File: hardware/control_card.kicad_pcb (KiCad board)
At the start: 6 copper layers, 32.5 x 33.8 mm, 144 parts, among them J1 Power board, J2 JTAG, U1 A3CZ065BB18AE7S, U10 SN74LV4051APWR, U11 OPA365AIDBVR, U12 ADS7056IRUGR, U13 SN74LV4051APWR, U14 OPA365AIDBVR, U15 ADS7056IRUGR, U16 TLV75518PDBVR, U2 AP61302Z6-7, U3 AP61102Z6-7, U4 AP61102Z6-7, U5 TLV75512PDBVR, U6 TLV75533PDBVR, U7 MT25QU256ABA8E12-1SIT, U8 SN74AVC4T774RSVR, U9 W958D8NBYA5I, X1 100MHz

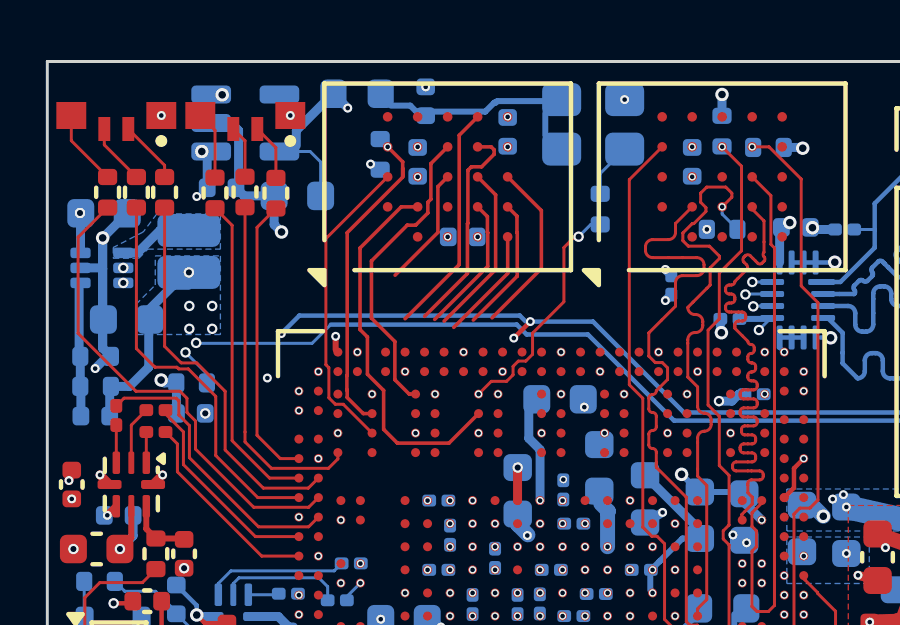
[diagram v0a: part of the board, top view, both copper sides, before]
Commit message: route hyperram to bank d for easier length matching
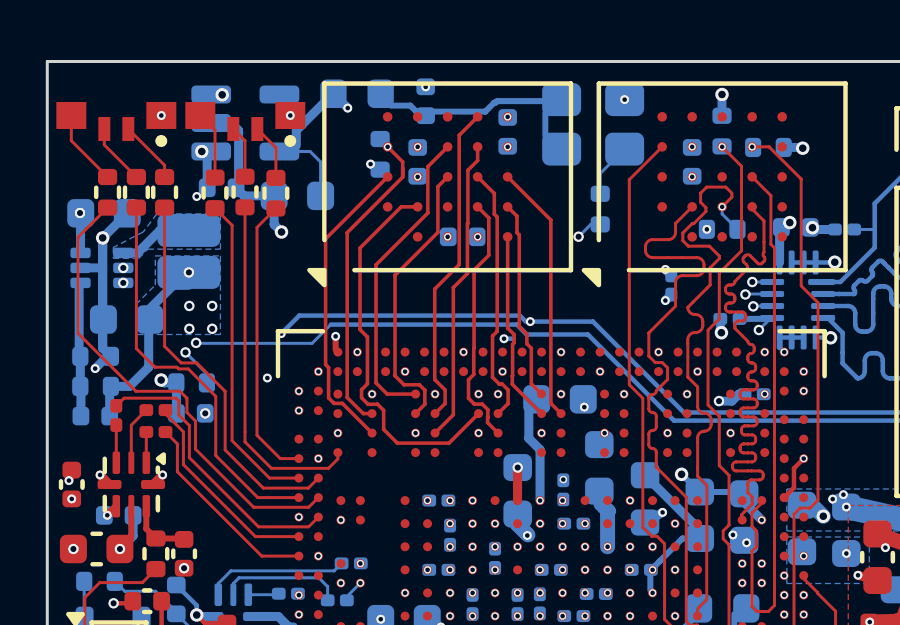
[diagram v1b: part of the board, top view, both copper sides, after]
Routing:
- net HR_RWDS: track 4.01 -> 9.46 mm
- net HR_DQ1: track 4.62 -> 8.54 mm
- net HR_DQ4: track 7.73 -> 10.8 mm
- net HR_DQ0: track 5.77 -> 8.64 mm
- net HR_DQ3: track 7.30 -> 10.1 mm
- net HR_DQ5: track 5.85 -> 8.63 mm
- net HR_DQ7: track 3.76 -> 6.41 mm
- net HR_DQ6: track 4.51 -> 6.71 mm
- net /Power/PG_1V8: track 47.6 -> 48.3 mm
